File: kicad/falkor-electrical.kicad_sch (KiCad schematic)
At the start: 3 parts, among them J1 Walstroomaansluiting, Y1 RF Antenne

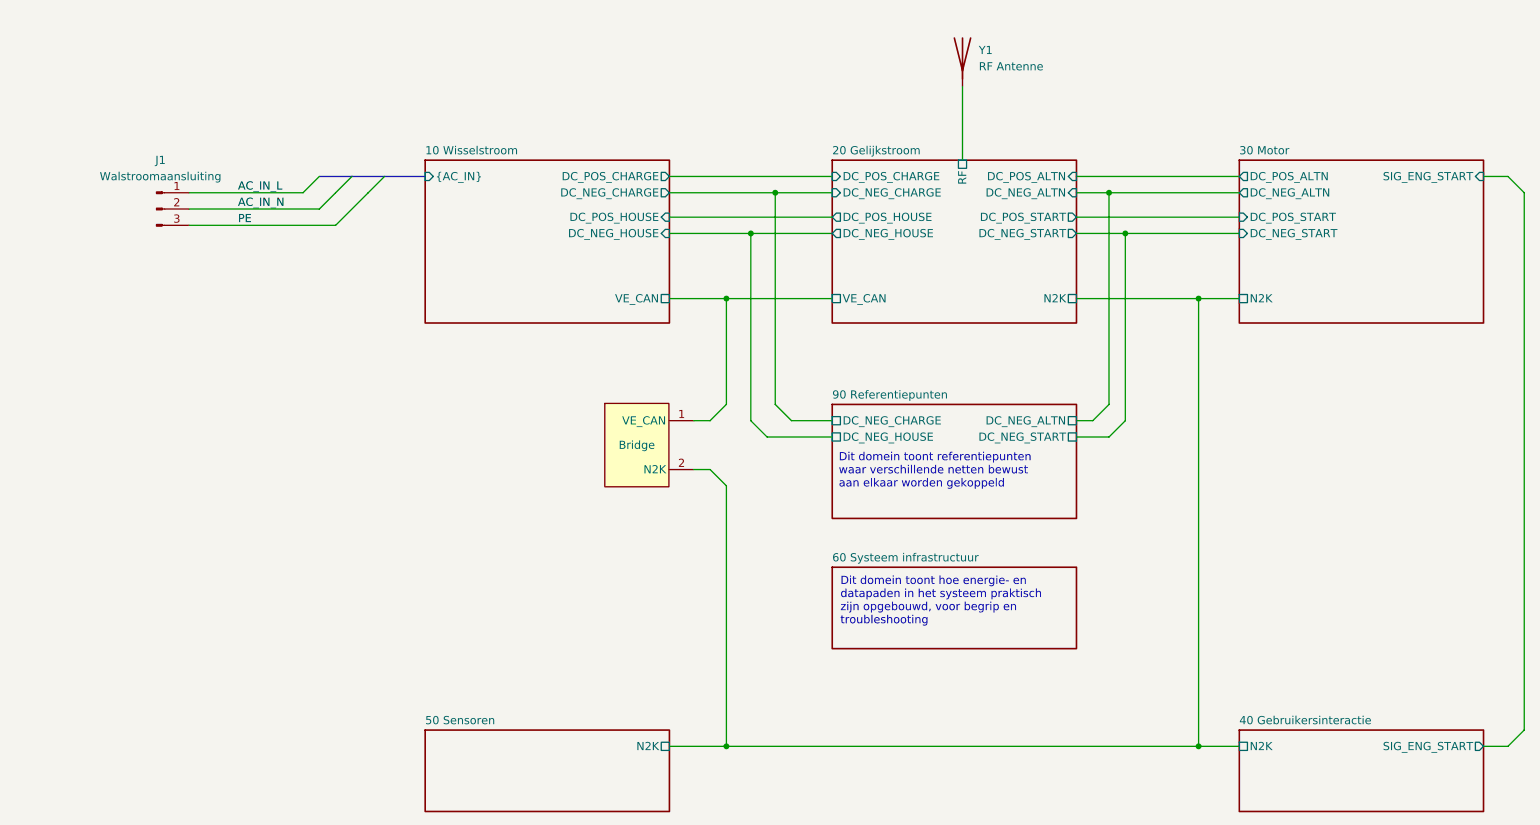
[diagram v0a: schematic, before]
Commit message: Introductie schema 15_energieconversie
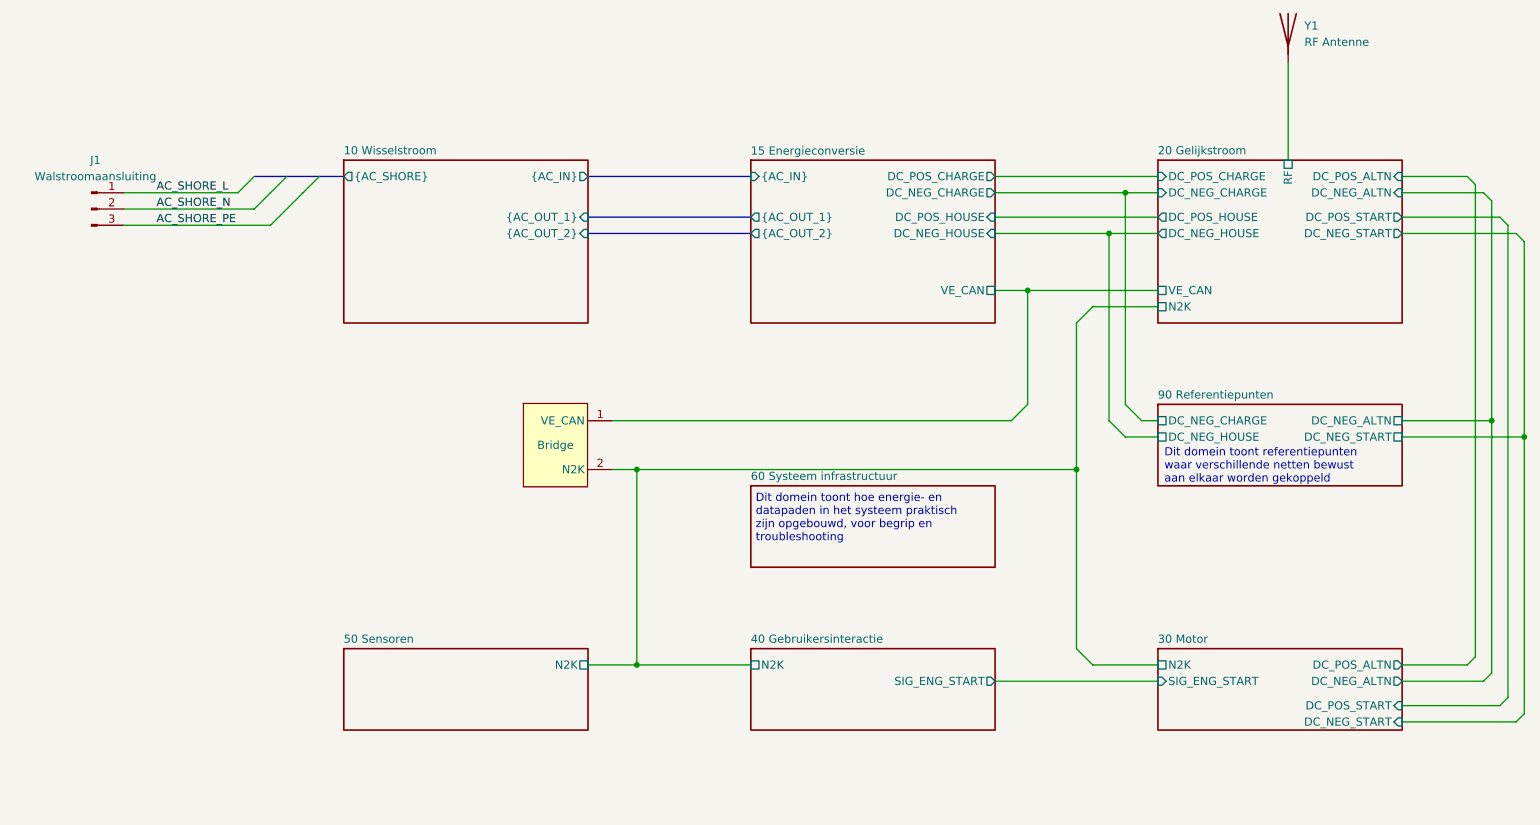
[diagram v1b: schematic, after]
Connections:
- net 10 Wisselstroom/VE_CAN renamed 15 Energieconversie/VE_CAN
- net AC_IN_L renamed AC_SHORE_L
- net AC_IN_N renamed AC_SHORE_N
- net PE renamed AC_SHORE_PE
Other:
- added sheet 15 Energieconversie (15_energieconversie.kicad_sch)
- sheet 10 Wisselstroom: file schematics\10_wisselstroom.kicad_sch -> schematics/10_wisselstroom.kicad_sch
- sheet 10 Wisselstroom ports: added {AC_OUT_1}, {AC_OUT_2}, {AC_SHORE}; removed DC_NEG_CHARGE, DC_NEG_HOUSE, DC_POS_CHARGE, DC_POS_HOUSE, VE_CAN
- sheet 20 Gelijkstroom: file schematics\20_gelijkstroom.kicad_sch -> schematics/20_gelijkstroom.kicad_sch
- sheet 30 Motor: file schematics\30_motor.kicad_sch -> schematics/30_motor.kicad_sch
- sheet 40 Gebruikersinteractie: file schematics\40_gebruikersinteractie.kicad_sch -> schematics/40_gebruikersinteractie.kicad_sch
- sheet 50 Sensoren: file schematics\50_sensoren.kicad_sch -> schematics/50_sensoren.kicad_sch
- sheet 60 Systeem infrastructuur: file schematics\60_systeem_infrastructuur.kicad_sch -> schematics/60_systeem_infrastructuur.kicad_sch
- sheet 90 Referentiepunten: file schematics\90_referentiepunten.kicad_sch -> schematics/90_referentiepunten.kicad_sch
- moved on the sheet: J1, Y1

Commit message: Schema's
00 toplevel stabiel
10 wisselstroom met subbladen stabiel
15 energieconversie stabiel
31 motor kern stabiel
32 motor sensoren stabiel
50 sensoren stabiel
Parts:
- removed ZZ1: Bridge, symbol falkor-electrical:Bridge_N2K_VEcan
- AE1: renamed from Y1; value RF Antenne -> Antenna
- J1: value Walstroomaansluiting -> Conn_01x03_Pin
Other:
- sheet 15 Energieconversie: file 15_energieconversie.kicad_sch -> schematics/15_energieconversie.kicad_sch
- sheet 15 Energieconversie ports: added N2K, PE; removed DC_NEG_CHARGE, DC_POS_CHARGE, VE_CAN
- sheet 20 Gelijkstroom ports: added none; removed DC_NEG_CHARGE, DC_POS_CHARGE, VE_CAN
- sheet 90 Referentiepunten ports: added PE; removed DC_NEG_CHARGE

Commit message: eerste opzet 21_laden_opslag_distributie
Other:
- sheet 20 Gelijkstroom ports: added DC_NEG_ALTERNATOR, DC_POS_ALTERNATOR; removed DC_NEG_ALTN, DC_POS_ALTN
- moved on the sheet: AE1
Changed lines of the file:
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@@
+	)
+	(junction
+		(at 247.65 93.98)
+		(diameter 0)
+		(color 0 0 0 0)
 	)
 	(junction
@@
 	)
 	(junction
-		(at 247.65 93.98)
-		(diameter 0)
-		(color 0 0 0 0)
-	)
-	(junction
 		(at 177.8 73.66)
 		(diameter 0)
@@
 	(wire
 		(pts
+			(xy 228.6 53.34) (xy 231.14 53.34)
+		)
+		(stroke
+			(width 0)
+			(type default)
+		)
+	)
+	(wire
+		(pts
 			(xy 123.19 93.98) (xy 190.5 93.98)
 		)
@@
 	(wire
 		(pts
-			(xy 228.6 53.34) (xy 238.76 53.34)
+			(xy 228.6 64.77) (xy 238.76 64.77)
 		)
 		(stroke
@@
 	(wire
 		(pts
-			(xy 242.57 57.15) (xy 241.3 55.88)
+			(xy 242.57 68.58) (xy 241.3 67.31)
 		)
 		(stroke
@@
 	(wire
 		(pts
-			(xy 210.82 35.56) (xy 210.82 50.8)
-		)
-		(stroke
-			(width 0)
-			(type default)
-		)
-	)
-	(wire
-		(pts
-			(xy 240.03 54.61) (xy 240.03 128.27)
+			(xy 240.03 66.04) (xy 240.03 128.27)
 		)
 		(stroke
@@
 	(wire
 		(pts
-			(xy 242.57 57.15) (xy 242.57 91.44)
+			(xy 242.57 68.58) (xy 242.57 91.44)
 		)
 		(stroke
@@
 	(wire
 		(pts
+			(xy 233.68 38.1) (xy 233.68 50.8)
+		)
+		(stroke
+			(width 0)
+			(type default)
+		)
+	)
+	(wire
+		(pts
 			(xy 120.65 68.58) (xy 123.19 66.04)
 		)
@@
 	(wire
 		(pts
-			(xy 228.6 59.69) (xy 243.84 59.69)
-		)
-		(stroke
-			(width 0)
-			(type default)
-		)
-	)
-	(wire
-		(pts
-			(xy 245.11 60.96) (xy 245.11 134.62)
-		)
-		(stroke
-			(width 0)
-			(type default)
-		)
-	)
-	(wire
-		(pts
-			(xy 228.6 62.23) (xy 246.38 62.23)
+			(xy 228.6 71.12) (xy 243.84 71.12)
+		)
+		(stroke
+			(width 0)
+			(type default)
+		)
+	)
+	(wire
+		(pts
+			(xy 245.11 72.39) (xy 245.11 134.62)
+		)
+		(stroke
+			(width 0)
+			(type default)
+		)
+	)
+	(wire
+		(pts
+			(xy 228.6 73.66) (xy 246.38 73.66)
 		)
 		(stroke
@@
 	(wire
 		(pts
-			(xy 238.76 53.34) (xy 240.03 54.61)
+			(xy 238.76 64.77) (xy 240.03 66.04)
 		)
 		(stroke
@@
 	(wire
 		(pts
-			(xy 243.84 59.69) (xy 245.11 60.96)
+			(xy 243.84 71.12) (xy 245.11 72.39)
 		)
 		(stroke
@@
 	(wire
 		(pts
+			(xy 231.14 53.34) (xy 233.68 50.8)
+		)
+		(stroke
+			(width 0)
+			(type default)
+		)
+	)
+	(wire
+		(pts
 			(xy 228.6 93.98) (xy 247.65 93.98)
 		)
@@
 	(wire
 		(pts
-			(xy 247.65 63.5) (xy 247.65 93.98)
+			(xy 247.65 74.93) (xy 247.65 93.98)
 		)
 		(stroke
@@
 	(wire
 		(pts
-			(xy 228.6 55.88) (xy 241.3 55.88)
+			(xy 228.6 67.31) (xy 241.3 67.31)
 		)
 		(stroke
@@
 	(wire
 		(pts
-			(xy 246.38 62.23) (xy 247.65 63.5)
+			(xy 246.38 73.66) (xy 247.65 74.93)
 		)
 		(stroke
@@
 	(symbol
 		(lib_id "Device:Antenna")
-		(at 210.82 30.48 0)
+		(at 233.68 33.02 0)
 		(unit 1)
 		(body_style 1)
@@
 		(fields_autoplaced yes)
 		(property "Reference" "AE1"
-			(at 213.36 29.8449 0)
+			(at 236.22 32.3849 0)
 			(show_name no)
 			(do_not_autoplace no)
@@
 		)
 		(property "Value" "Antenna"
-			(at 213.36 32.3849 0)
+			(at 236.22 34.9249 0)
 			(show_name no)
 			(do_not_autoplace no)
@@
 		)
 		(property "Footprint" ""
-			(at 210.82 30.48 0)
+			(at 233.68 33.02 0)
 			(hide yes)
 			(show_name no)
@@
 		)
 		(property "Datasheet" ""
-			(at 210.82 30.48 0)
+			(at 233.68 33.02 0)
 			(hide yes)
 			(show_name no)
@@
 		)
 		(property "Description" "Antenna"
-			(at 210.82 30.48 0)
+			(at 233.68 33.02 0)
 			(hide yes)
 			(show_name no)
@@
 			)
 		)
-		(pin "DC_NEG_ALTN" input
-			(at 228.6 55.88 0)
+		(pin "DC_NEG_ALTERNATOR" input
+			(at 228.6 67.31 0)
 			(effects
 				(font
@@
 		)
 		(pin "DC_POS_START" output
-			(at 228.6 59.69 0)
-			(effects
-				(font
-					(size 1.27 1.27)
-				)
-				(justify right)
-			)
-		)
-		(pin "DC_POS_ALTN" input
-			(at 228.6 53.34 0)
+			(at 228.6 71.12 0)
+			(effects
+				(font
+					(size 1.27 1.27)
+				)
+				(justify right)
+			)
+		)
+		(pin "DC_POS_ALTERNATOR" input
+			(at 228.6 64.77 0)
 			(effects
 				(font
@@
 		)
 		(pin "DC_NEG_START" output
-			(at 228.6 62.23 0)
+			(at 228.6 73.66 0)
 			(effects
 				(font
@@
 		)
 		(pin "RF" passive
-			(at 210.82 50.8 90)
-			(effects
-				(font
+			(at 228.6 53.34 0)
+			(effects
+				(font
